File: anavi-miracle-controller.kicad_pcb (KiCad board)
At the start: 2 copper layers, 74.9 x 40.6 mm, 31 parts, among them J1 INPUT, P1 CONN_01X03, T1 Screw_Terminal_01x06, U1 I2C_SENS_1, U2 I2C_SENS_1, U3 I2C_SENS_1

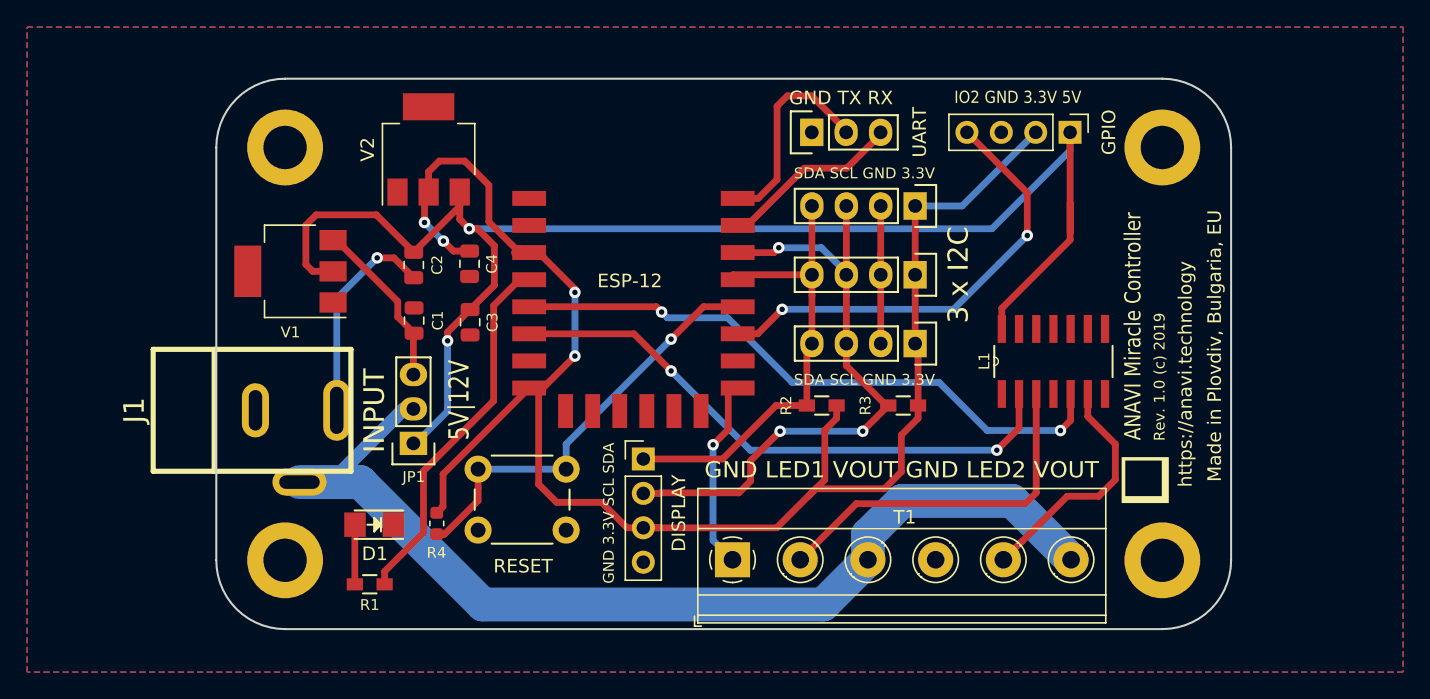
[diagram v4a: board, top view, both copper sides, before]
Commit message: Revision 1.1: Fix DC Jack
Update the schedatics, fix the DC jack on the PCB.

Signed-off-by: Leon Anavi <leon@anavi.org>
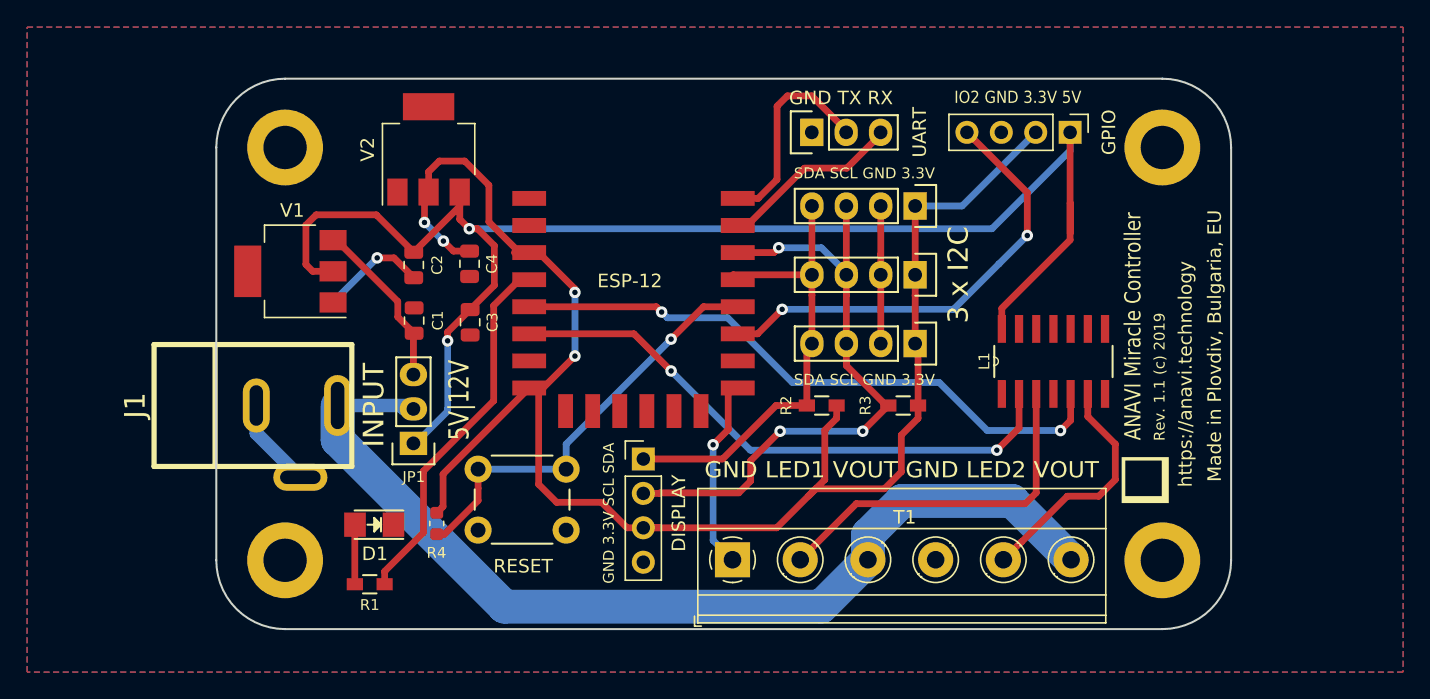
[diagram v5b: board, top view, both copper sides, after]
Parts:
- V2: value NCP1117ST33T3G -> LD1117S33TR
- moved J1 0.36 mm to (67.5, 95.2)
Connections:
- J1 pad 1: Net-(J1-Pad1) -> GND
- J1 pad 3: GND -> Net-(J1-Pad3)
- JP1 pad 2: Net-(J1-Pad1) -> Net-(J1-Pad3)
- T1 pad 3: Net-(J1-Pad1) -> Net-(J1-Pad3)
- T1 pad 6: Net-(J1-Pad1) -> Net-(J1-Pad3)
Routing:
- net Net-(J1-Pad1): track 77.6 -> 0.00 mm
- net Net-(J1-Pad3): track 0.00 -> 74.4 mm
- net GND: track 41.2 -> 38.3 mm
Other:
- board text added: "Rev. 1.1 (c) 2019"
- board text removed: "Rev. 1.0 (c) 2019"

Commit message: anavi-miracle-controller.kicad_pcb: Assembly
Update assembly guidelines on the board.

Signed-off-by: Leon Anavi <leon@anavi.org>
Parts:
- V2: value LD1117S33TR -> NCP1117ST33T3G
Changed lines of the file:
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@@
       (effects (font (size 0.8 0.8) (thickness 0.15)))
     )
-    (fp_text value 68R (at -3.45 -0.7 180) (layer F.Fab)
+    (fp_text value 68R (at 3.025 -1.55 180) (layer F.Fab)
       (effects (font (size 1 1) (thickness 0.15)))
     )
@@
       (effects (font (size 0.8 0.8) (thickness 0.1)))
     )
-    (fp_text value 4,7K (at 0.084 1.524 180) (layer F.Fab)
+    (fp_text value 4,7K (at -0.001 -1.6 180) (layer F.Fab)
       (effects (font (size 1 1) (thickness 0.15)))
     )
@@
       (effects (font (size 0.8 0.8) (thickness 0.1)))
     )
-    (fp_text value 4,7K (at 0 1.27 180) (layer F.Fab)
+    (fp_text value 4,7K (at 0.011 -1.6 180) (layer F.Fab)
       (effects (font (size 1 1) (thickness 0.15)))
     )
@@
       (effects (font (size 0.8 0.8) (thickness 0.15)))
     )
-    (fp_text value 2K (at 1.4375 1.45 90) (layer F.Fab)
+    (fp_text value 2K (at 2.5875 0 90) (layer F.Fab)
       (effects (font (size 1 1) (thickness 0.15)))
     )
@@
       (effects (font (size 1 1) (thickness 0.15)))
     )
-    (fp_text value LD1117S33TR (at 0 4.5 90) (layer F.Fab)
+    (fp_text value NCP1117ST33T3G (at 0 4.5 90) (layer F.Fab)
       (effects (font (size 0.8 0.8) (thickness 0.1)))
     )
